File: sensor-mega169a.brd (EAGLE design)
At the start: 55.6 x 39.9 mm, 59 parts, among them IC3 ATmega169PA, K1 SP6029TOP, M1 NRF24L01P-M, M2 DHT22, Q1 IRLML2502, Q2 IRLML2502, Q3 IRLML6402, U1 MCP1640C, U2 MCP604-I/ST

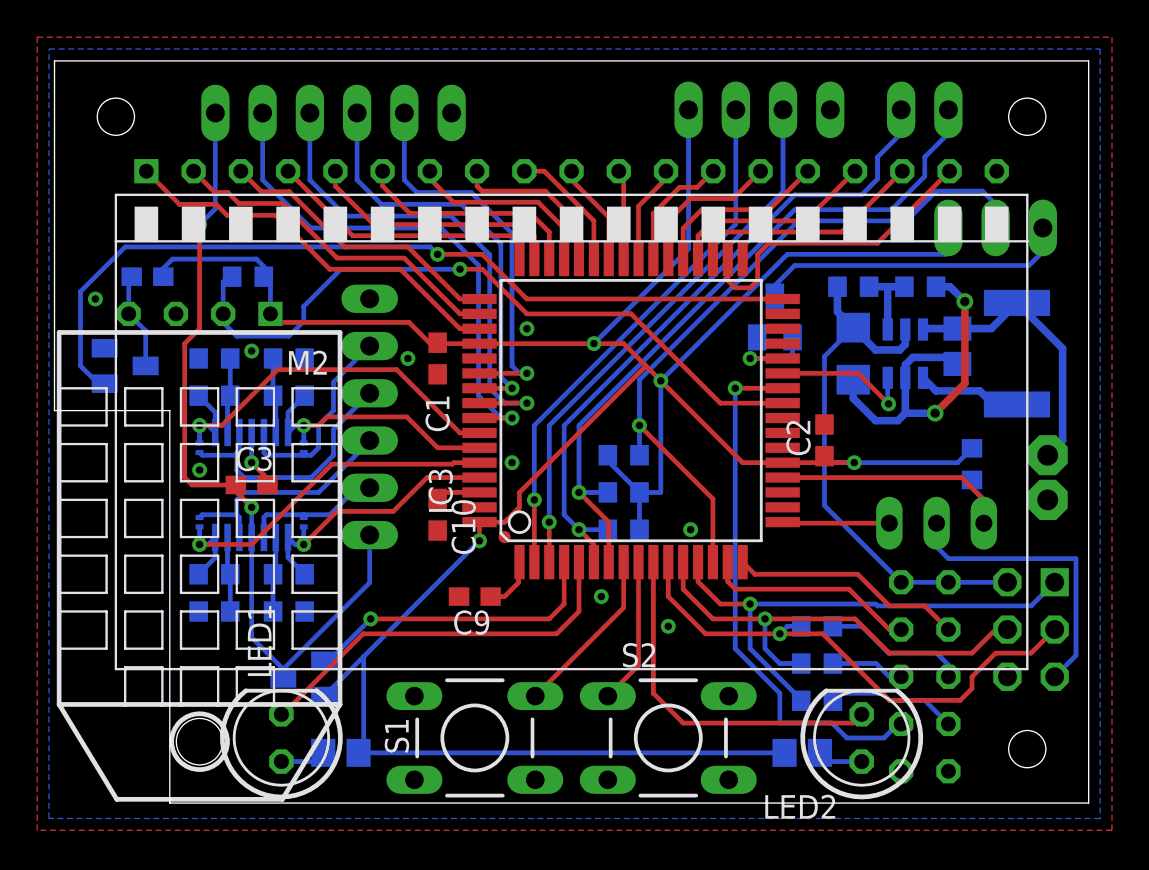
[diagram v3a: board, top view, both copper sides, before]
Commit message: rearranged some wires
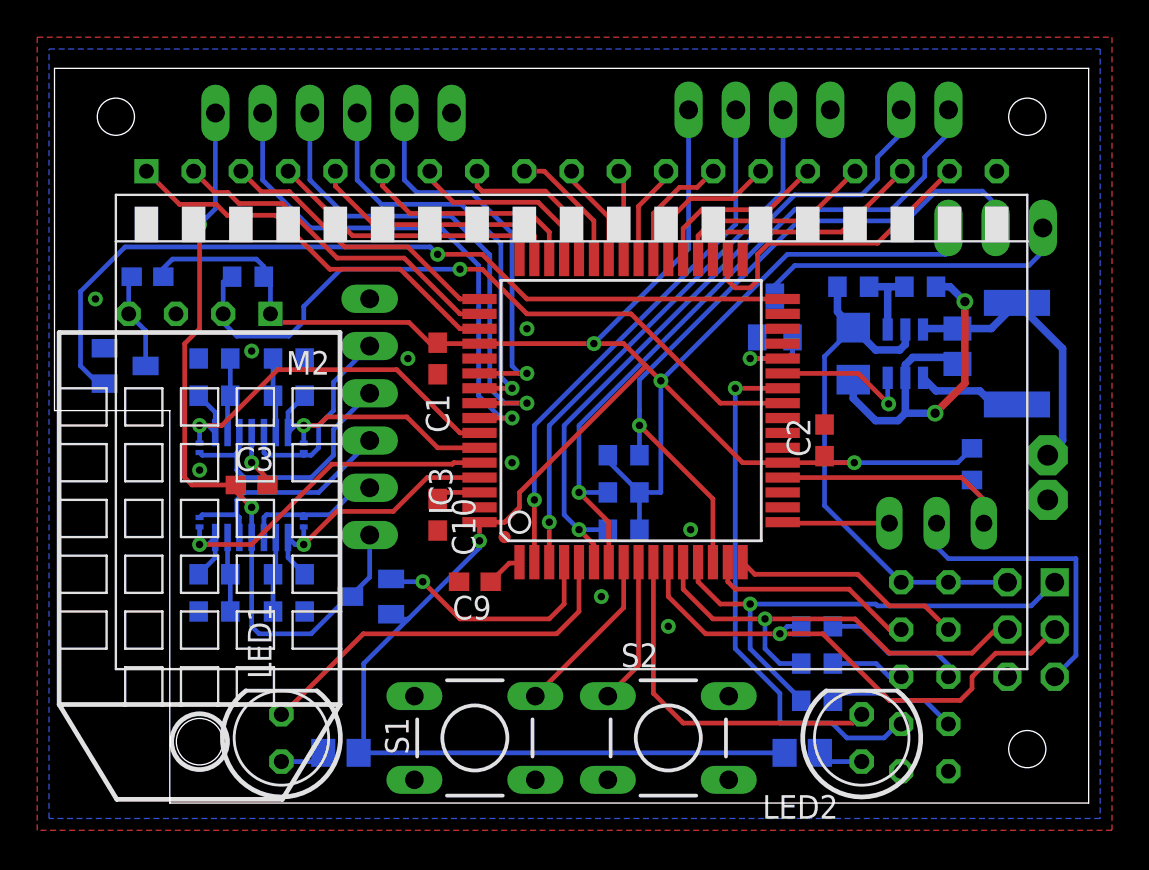
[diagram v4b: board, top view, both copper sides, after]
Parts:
- moved Q3 5.69 mm to (17.2, 13.2)
- moved U$1 1.60 mm to (37.2, 10.0)
- moved U$3 1.60 mm to (32.0, 10.0)
- moved U$4 1.60 mm to (26.8, 10.0)
- moved C9 0.80 mm to (22.8, 14.0)
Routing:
- net ADCON: track 16.4 -> 12.8 mm
- net N$17: track 44.3 -> 41.7 mm
- net VCC: track 180.9 -> 179.0 mm
- net LCDCAP: track 2.93 -> 1.98 mm
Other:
- board size 55.6 x 39.9 mm -> 55.6 x 39.5 mm
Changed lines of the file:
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@@
 <layer number="45" name="Holes" color="7" fill="1" visible="no" active="yes"/>
 <layer number="46" name="Milling" color="3" fill="1" visible="yes" active="yes"/>
-<layer number="47" name="Measures" color="7" fill="1" visible="no" active="yes"/>
-<layer number="48" name="Document" color="7" fill="1" visible="no" active="yes"/>
-<layer number="49" name="Reference" color="7" fill="1" visible="no" active="yes"/>
+<layer number="47" name="Measures" color="7" fill="1" visible="yes" active="yes"/>
+<layer number="48" name="Document" color="7" fill="1" visible="yes" active="yes"/>
+<layer number="49" name="Reference" color="7" fill="1" visible="yes" active="yes"/>
 <layer number="50" name="dxf" color="7" fill="1" visible="no" active="no"/>
 <layer number="51" name="tDocu" color="7" fill="1" visible="no" active="yes"/>
@@
 <wire x1="6.4" y1="23.2" x2="6.4" y2="2.1" width="0" layer="20"/>
 <wire x1="6.4" y1="2.1" x2="55.8" y2="2.1" width="0" layer="20"/>
-<wire x1="55.8" y1="2.1" x2="55.8" y2="42" width="0" layer="20"/>
-<wire x1="55.8" y1="42" x2="0.2" y2="42" width="0" layer="20"/>
-<wire x1="0.2" y1="42" x2="0.2" y2="23.2" width="0" layer="20"/>
+<wire x1="55.8" y1="2.1" x2="55.8" y2="41.6" width="0" layer="20"/>
+<wire x1="55.8" y1="41.6" x2="0.2" y2="41.6" width="0" layer="20"/>
+<wire x1="0.2" y1="41.6" x2="0.2" y2="23.2" width="0" layer="20"/>
 <wire x1="0.2" y1="23.2" x2="6.4" y2="23.2" width="0" layer="20"/>
 <hole x="52.5" y="5" drill="2"/>
@@
 <element name="DISP1" library="lcd_displays" package="DE325" value="DE325" x="28" y="34.8" locked="yes"/>
 <element name="C2" library="rcl" package="C0603" value="100n" x="41.6" y="21.6" rot="R90"/>
-<element name="C9" library="rcl" package="C0603" value="1u" x="22.8" y="13.2" rot="R180"/>
+<element name="C9" library="rcl" package="C0603" value="1u" x="22.8" y="14" rot="R180"/>
 <element name="C10" library="rcl" package="C0603" value="100n" x="20.8" y="17.6" rot="R270"/>
 <element name="U1" library="karlnet-parts" package="SOT23-6" value="MCP1640C" x="45.945" y="26.26" rot="MR0"/>
@@
 <element name="R23" library="rcl" package="R0201" value="0" x="13.6" y="21.2" rot="MR90"/>
 <element name="R24" library="rcl" package="R0201" value="0" x="8" y="21.2" rot="MR90"/>
-<element name="Q3" library="mosfet" package="MICRO3" value="IRLML6402" x="13.6" y="8.8" rot="MR270"/>
+<element name="Q3" library="mosfet" package="MICRO3" value="IRLML6402" x="17.2" y="13.2" rot="MR270"/>
 <element name="JP4" library="pinhead-mod" package="1X06" value="ADC1" x="17.145" y="22.86" locked="yes" rot="MR90"/>
 <element name="JP5" library="pinhead-mod" package="1X06" value="ADC2" x="15.2" y="39.2" rot="MR180"/>
-<element name="U$1" library="creative-commons" package="CC_TPLACE_HS" value="CC-TPLACE-HALF" x="35.6" y="10" rot="MR0"/>
-<element name="U$3" library="creative-commons" package="BY_TPLACE_HS" value="BY-TPLACE-HS" x="30.4" y="10" rot="MR0"/>
-<element name="U$4" library="creative-commons" package="SA_TPLACE_HS" value="SA-TPLACE-HALF" x="25.2" y="10" rot="MR0"/>
+<element name="U$1" library="creative-commons" package="CC_TPLACE_HS" value="CC-TPLACE-HALF" x="37.2" y="10" rot="MR0"/>
+<element name="U$3" library="creative-commons" package="BY_TPLACE_HS" value="BY-TPLACE-HS" x="32" y="10" rot="MR0"/>
+<element name="U$4" library="creative-commons" package="SA_TPLACE_HS" value="SA-TPLACE-HALF" x="26.8" y="10" rot="MR0"/>
 <element name="JP6" library="jumper" package="JP2" value="" x="47.625" y="17.145" rot="MR180"/>
 </elements>
@@
 <wire x1="49.53" y1="21.17" x2="48.76" y2="20.4" width="0.254" layer="16"/>
 <wire x1="48.76" y1="20.4" x2="43.2" y2="20.4" width="0.254" layer="16"/>
-<wire x1="14.7" y1="7.85" x2="16.825" y2="9.975" width="0.254" layer="16"/>
-<wire x1="16.825" y1="9.975" x2="23.05" y2="16.2" width="0.254" layer="16"/>
 <wire x1="23.05" y1="16.2" x2="23.05" y2="17.2" width="0.254" layer="1"/>
 <via x="23.05" y="16.2" extent="1-16" drill="0.4"/>
 <wire x1="16.55" y1="4.8" x2="16.825" y2="5.075" width="0.254" layer="16"/>
-<wire x1="16.825" y1="5.075" x2="16.825" y2="9.975" width="0.254" layer="16"/>
+<wire x1="16.825" y1="5.075" x2="16.825" y2="9.6" width="0.254" layer="16"/>
+<wire x1="18.3" y1="12.25" x2="18.3" y2="12.1" width="0.254" layer="16"/>
+<wire x1="23.05" y1="16.2" x2="23.05" y2="15.825" width="0.254" layer="16"/>
+<wire x1="23.05" y1="15.825" x2="19.2125" y2="11.9875" width="0.254" layer="16"/>
+<wire x1="19.2125" y1="11.9875" x2="16.825" y2="9.6" width="0.254" layer="16"/>
+<wire x1="18.3" y1="12.1" x2="18.4125" y2="11.9875" width="0.254" layer="16"/>
+<wire x1="18.4125" y1="11.9875" x2="19.2125" y2="11.9875" width="0.254" layer="16"/>
 </signal>
 <signal name="RFCE">
@@
 <contactref element="C9" pad="1"/>
 <wire x1="25.15" y1="15" x2="25.2" y2="15.05" width="0.254" layer="1"/>
-<wire x1="25.15" y1="15" x2="25.15" y2="13.95" width="0.254" layer="1"/>
-<wire x1="25.15" y1="13.95" x2="24.4" y2="13.2" width="0.254" layer="1"/>
-<wire x1="24.4" y1="13.2" x2="23.65" y2="13.2" width="0.254" layer="1"/>
+<wire x1="25.15" y1="15" x2="24.65" y2="15" width="0.254" layer="1"/>
+<wire x1="24.65" y1="15" x2="23.65" y2="14" width="0.254" layer="1"/>
 </signal>
 <signal name="AREF">
@@
 <wire x1="7.6" y1="19.2" x2="9.95" y2="19.2" width="0.254" layer="1"/>
 <via x="8" y="33.2" extent="1-16" drill="0.4"/>
-<wire x1="17.145" y1="13.945" x2="17.145" y2="16.51" width="0.254" layer="16"/>
 <wire x1="8.85" y1="39.2" x2="8.85" y2="34.05" width="0.254" layer="16"/>
 <wire x1="8.85" y1="34.05" x2="8" y2="33.2" width="0.254" layer="16"/>
-<wire x1="10.8" y1="16.3806" x2="10.8" y2="11" width="0.254" layer="16"/>
-<wire x1="17.145" y1="13.945" x2="12.5" y2="9.3" width="0.254" layer="16"/>
-<wire x1="12.5" y1="9.3" x2="12.5" y2="8.8" width="0.254" layer="16"/>
-<wire x1="10.8" y1="11" x2="12.5" y2="9.3" width="0.254" layer="16"/>
+<wire x1="10.8" y1="16.3806" x2="10.8" y2="11.6" width="0.254" layer="16"/>
+<wire x1="17.145" y1="16.51" x2="17.145" y2="14.245" width="0.254" layer="16"/>
+<wire x1="17.145" y1="14.245" x2="16.1" y2="13.2" width="0.254" layer="16"/>
+<wire x1="16.1" y1="13.2" x2="16" y2="13.2" width="0.254" layer="16"/>
+<wire x1="16" y1="13.2" x2="14" y2="11.2" width="0.254" layer="16"/>
+<wire x1="14" y1="11.2" x2="11.2" y2="11.2" width="0.254" layer="16"/>
+<wire x1="11.2" y1="11.2" x2="10.8" y2="11.6" width="0.254" layer="16"/>
 </signal>
 <signal name="N$16">
@@
 <contactref element="Q3" pad="1"/>
 <wire x1="27.6" y1="12.8" x2="26.8" y2="12" width="0.254" layer="1"/>
-<wire x1="26.8" y1="12" x2="17.2" y2="12" width="0.254" layer="1"/>
-<via x="17.2" y="12" extent="1-16" drill="0.4"/>
+<wire x1="26.8" y1="12" x2="22" y2="12" width="0.254" layer="1"/>
 <contactref element="IC3" pad="4"/>
 <wire x1="27.6" y1="12.8" x2="27.6" y2="15.05" width="0.254" layer="1"/>
-<wire x1="17.2" y1="12" x2="14.95" y2="9.75" width="0.254" layer="16"/>
-<wire x1="14.95" y1="9.75" x2="14.7" y2="9.75" width="0.254" layer="16"/>
+<wire x1="22" y1="12" x2="20" y2="14" width="0.254" layer="1"/>
+<via x="20" y="14" extent="1-16" drill="0.4"/>
+<wire x1="20" y1="14" x2="18.45" y2="14" width="0.254" layer="16"/>
+<wire x1="18.45" y1="14" x2="18.3" y2="14.15" width="0.254" layer="16"/>
 </signal>
 <signal name="DHTON">
